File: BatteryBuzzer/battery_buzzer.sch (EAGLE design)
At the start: 20 parts, among them Q1 IRFML8244, Q2 IRFML8244, Q3 P-CHANNEL-MOSFETSOT23-3, Q4 P-CHANNEL-MOSFETSOT23-3, Q5 P-CHANNEL-MOSFETSOT23-3

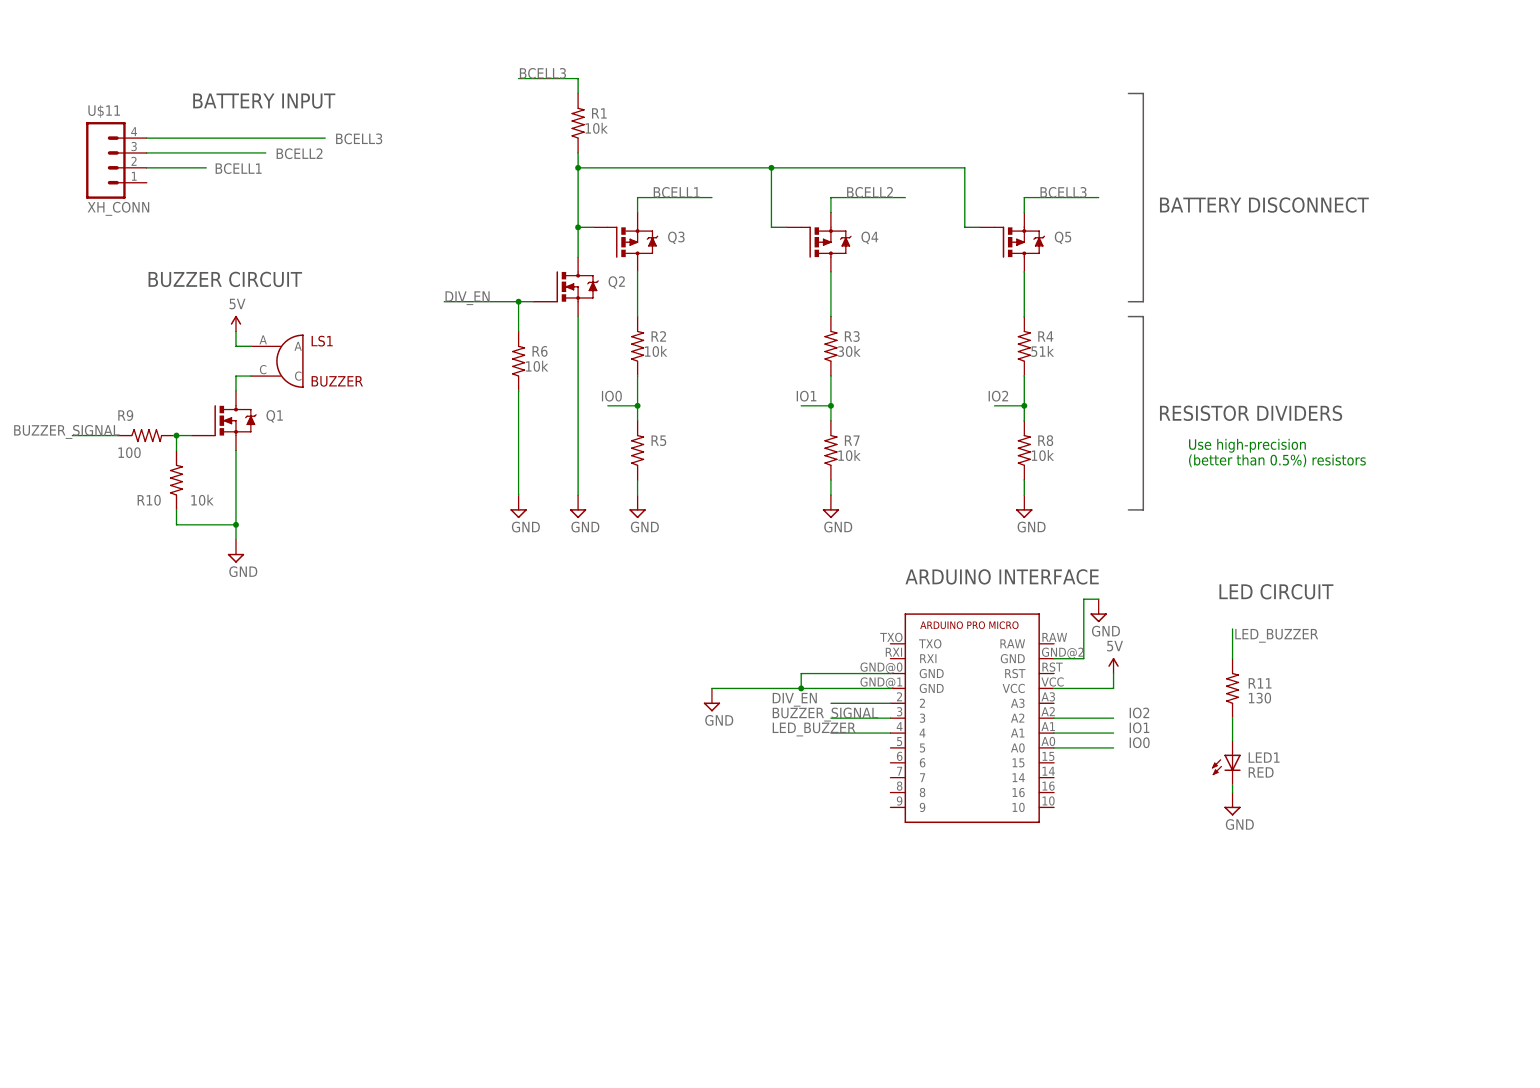
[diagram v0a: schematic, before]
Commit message: Added 7 segment array & calibration.
also nuked board file, it'd have to change too much anyway.

Have just enough I/O for the calibration button + calibration button
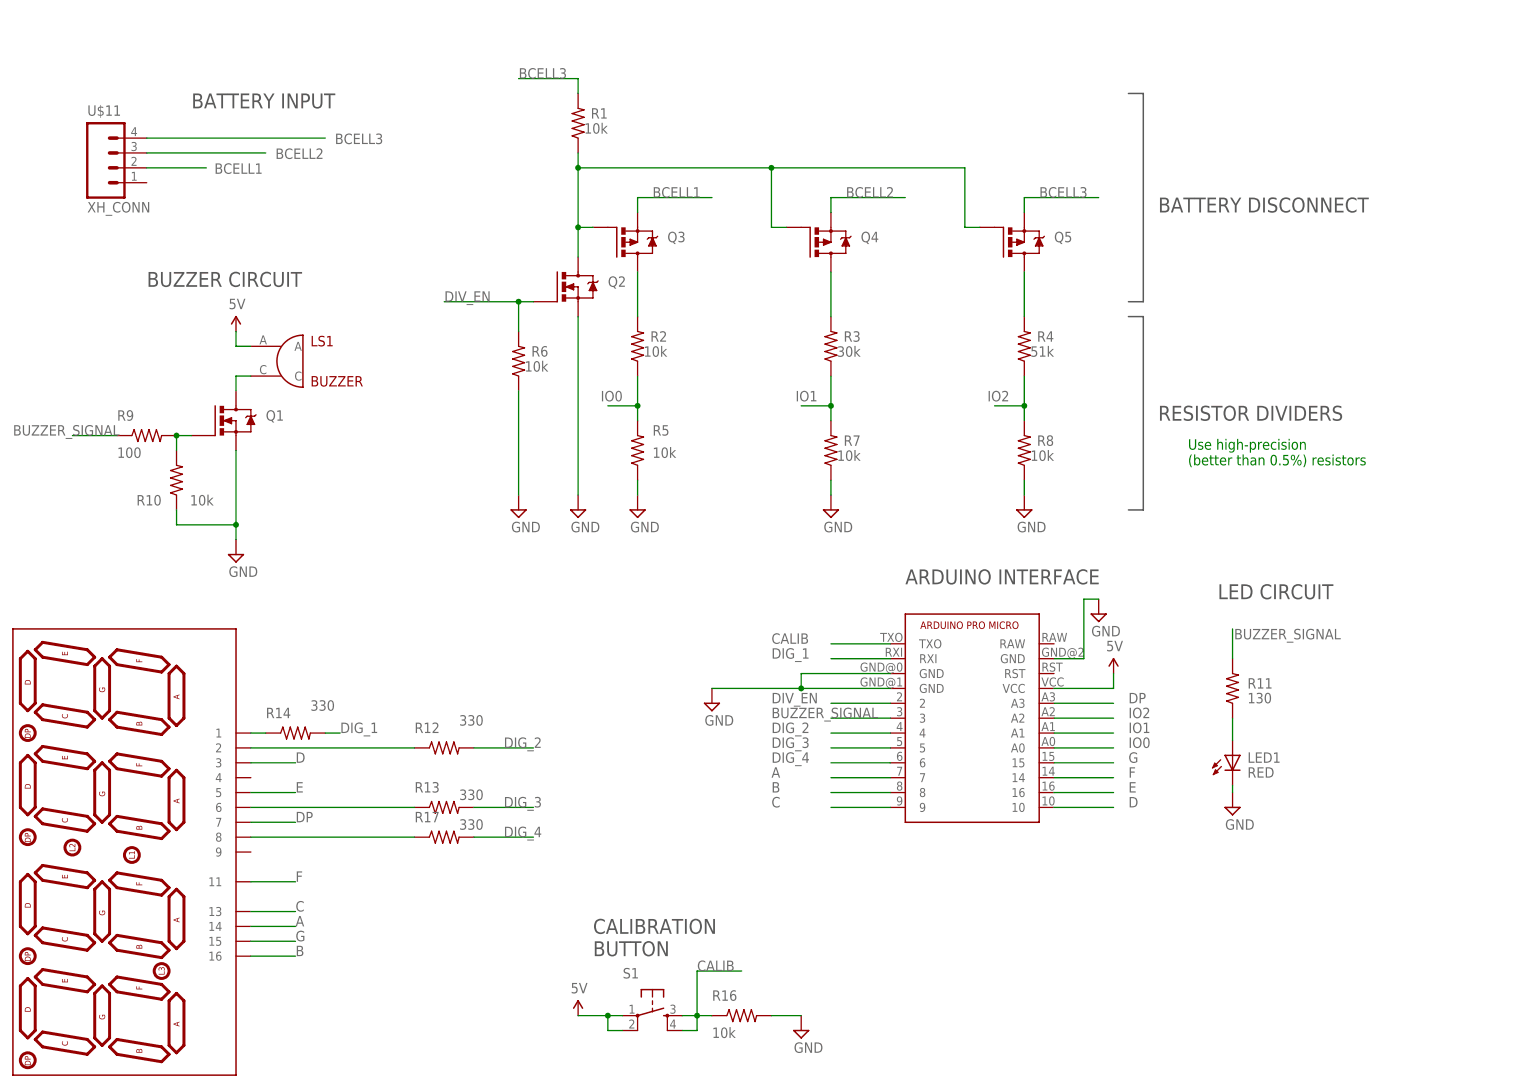
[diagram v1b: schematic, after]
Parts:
- added R12, R13, R14, R17: 330, pie:R-US_R0603
- added R16: 10k, pie:R-US_R0603
- added S1: (no value), pie:TAC_SWITCHPTH
- added U$6: 7-SEGMENT-4DIGIT, SparkFun-Displays:7-SEGMENT-4DIGIT
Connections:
- removed net LED_BUZZER: R11.2, U$5.4
- new net A: U$5.7, U$6.14
- new net B: U$5.8, U$6.16
- new net C: U$5.9, U$6.13
- new net CALIB: R16.1, S1.3, S1.4, U$5.TXO
- new net D: U$5.10, U$6.3
- new net DIG_1: R14.2, U$5.RXI
- new net DIG_2: R12.2, U$5.4
- new net DIG_3: R13.2, U$5.5
- new net DIG_4: R17.2, U$5.6
- new net DP: U$5.A3, U$6.7
- new net E: U$5.16, U$6.5
- new net F: U$5.14, U$6.11
- new net G: U$5.15, U$6.15
- new net N$10: R13.1, U$6.6
- new net N$12: R17.1, U$6.8
- new net N$14: R14.1, U$6.1
- new net N$8: R12.1, U$6.2
- net 5V: now also S1.1, S1.2
- net BUZZER_SIGNAL: now also R11.2
- net GND: now also R16.2
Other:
- note added: "CALIBRATION BUTTON"

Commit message: added DPST switch to libary, added power bypass to buzzer
power bypass so that with the push of a button the buzzer can turn out
powered by the battery alone.
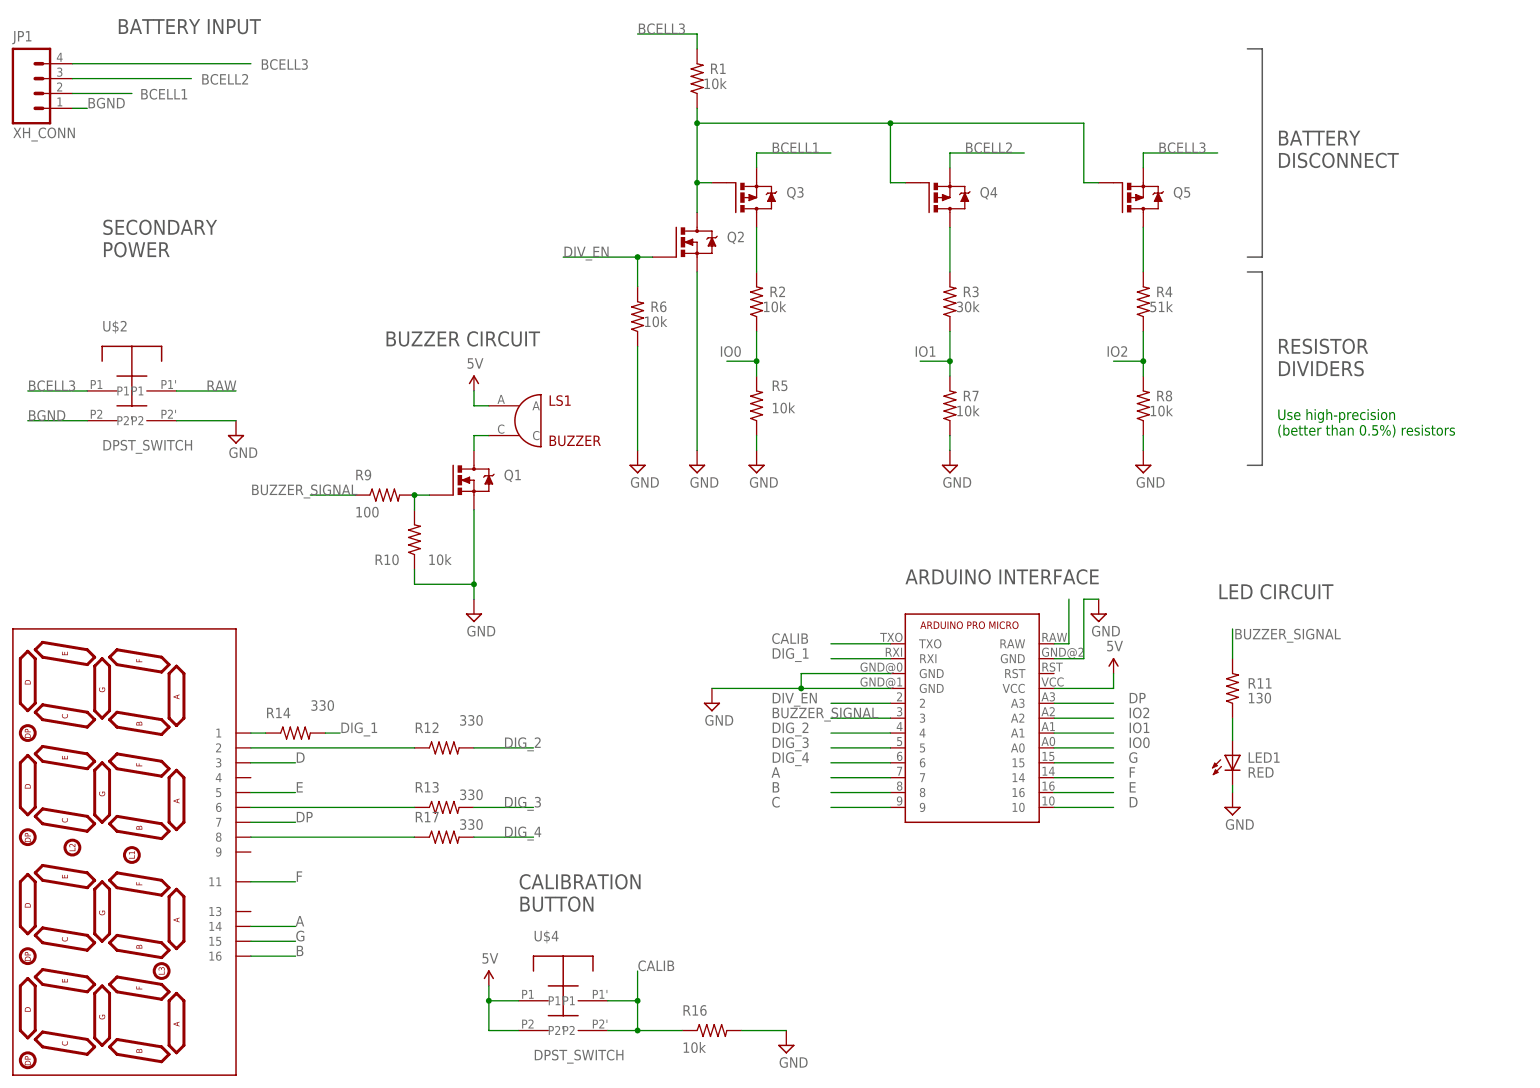
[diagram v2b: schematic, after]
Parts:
- removed S1: (no value), pie:TAC_SWITCHPTH
- removed U$11: XH_CONN, pie:XH_CONNECTOR_4POS
- added JP1: XH_CONN, pie:XH_CONNECTOR_4POS
- added U$2, U$4: DPST_SWITCH, pie:DPST_SWITCH
- renumbered U$5 to UC1, U$6 to DISP
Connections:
- new net BGND: JP1.1, U$2.P2
- new net RAW: U$2.P1', UC1.RAW
- net 5V: now also U$4.P1, U$4.P2; no longer S1.1, S1.2
- net BCELL1: now also JP1.2; no longer U$11.2
- net BCELL2: now also JP1.3; no longer U$11.3
- net BCELL3: now also JP1.4, U$2.P1; no longer U$11.4
- net C: no longer DISP.13
- net CALIB: now also U$4.P1', U$4.P2'; no longer S1.3, S1.4
- net GND: now also U$2.P2'
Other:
- note added: "DPST switch. Connect BCELL3 to RAW, which will get regulated on the arduino. Connect BGND to GND."
- note added: "SECONDARY POWER"
- moved on the sheet: LS1, Q1, Q2, Q3, Q4, Q5, R1, R10, R16, R2, R3, R4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

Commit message: final additions to the battery buzzer schematic
cleaned things up, added the obligatory debug features.
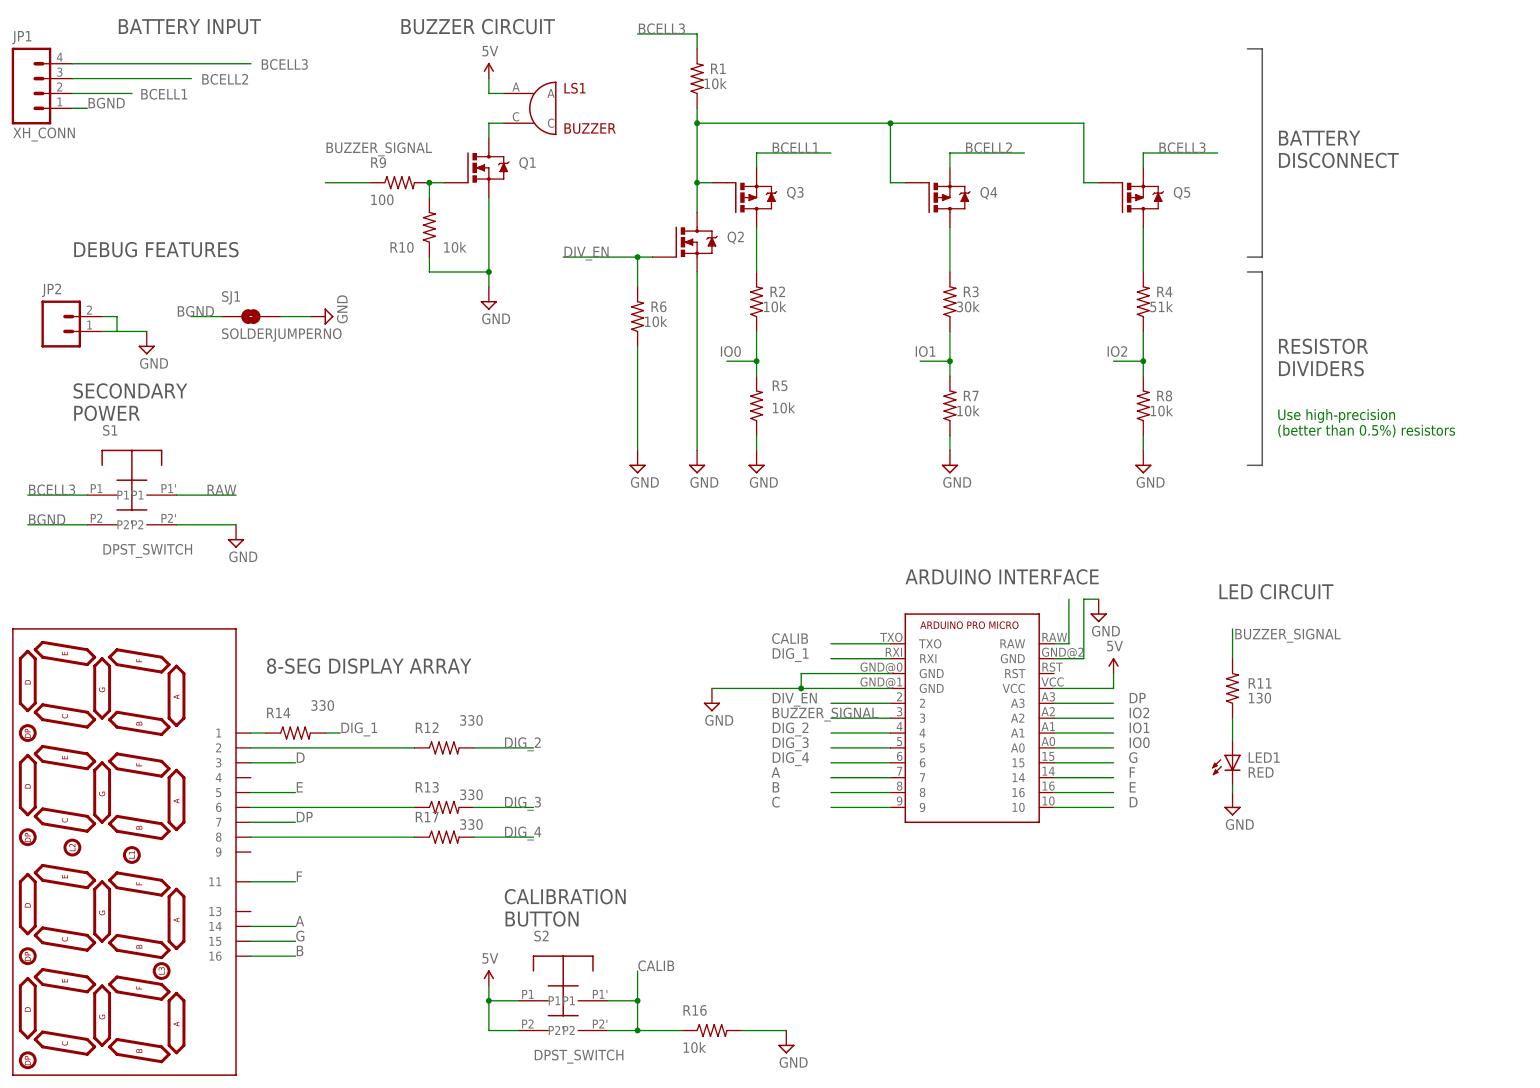
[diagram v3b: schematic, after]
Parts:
- removed U$2: DPST_SWITCH, pie:DPST_SWITCH
- added JP2: (no value), pie:M02PTH
- added S1: DPST_SWITCH, pie:DPST_SWITCH
- added SJ1: SOLDERJUMPERNO, pie:SOLDERJUMPERNO
- renumbered U$4 to S2
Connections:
- net BCELL3: now also S1.P1; no longer U$2.P1
- net BGND: now also S1.P2, SJ1.1; no longer U$2.P2
- net GND: now also JP2.1, JP2.2, S1.P2', SJ1.2; no longer U$2.P2'
- net RAW: now also S1.P1'; no longer U$2.P1'
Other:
- note added: "8-SEG DISPLAY ARRAY"
- note added: "Connect BCELL3 to RAW, which will get regulated on the arduino."
- note added: "DEBUG FEATURES"
- note removed: "DPST switch. Connect BCELL3 to RAW, which will get regulated on the arduino. Connect BGND to GND."
- note removed: "Do not connect ground pin on this battery leads unless it has a corrisponding reverse-plugin disconnect: it will short 12V to GND else"
- moved on the sheet: LS1, Q1, R10, R9

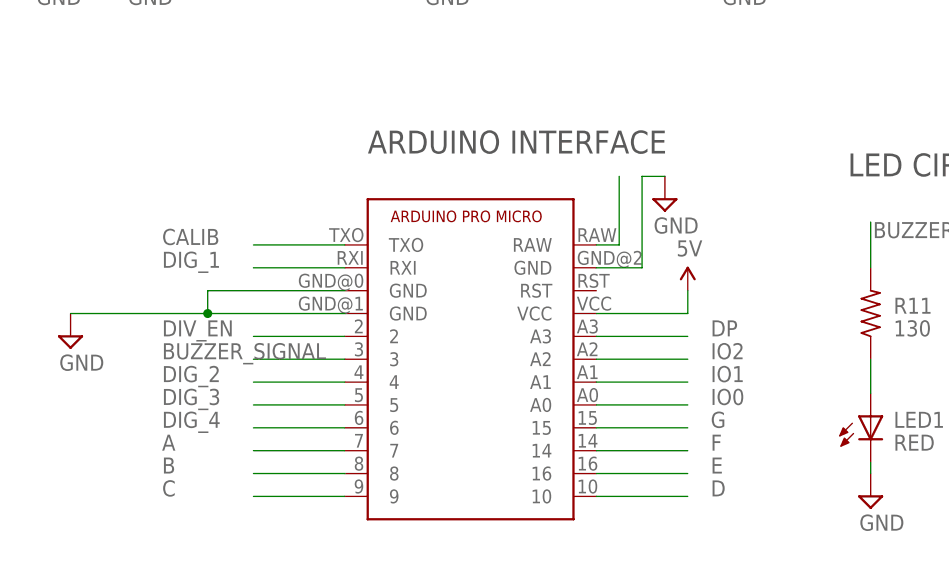
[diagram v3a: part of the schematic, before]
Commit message: some more pinremapping
to make routing easier... but routing starting now.
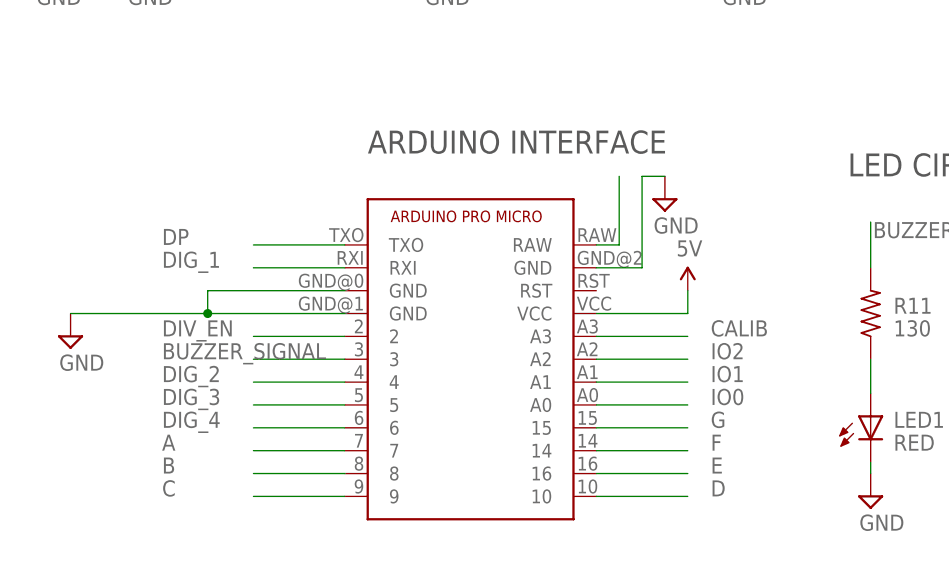
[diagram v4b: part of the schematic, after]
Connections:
- net CALIB: now also UC1.A3; no longer UC1.TXO
- net DP: now also UC1.TXO; no longer UC1.A3
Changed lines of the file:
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@@
 </segment>
 <segment>
-<pinref part="UC1" gate="G$1" pin="A3"/>
-<wire x1="180.34" y1="66.04" x2="190.5" y2="66.04" width="0.1524" layer="91"/>
-<label x="193.04" y="66.04" size="1.778" layer="95"/>
+<pinref part="UC1" gate="G$1" pin="TXO"/>
+<wire x1="152.4" y1="76.2" x2="142.24" y2="76.2" width="0.1524" layer="91"/>
+<label x="132.08" y="76.2" size="1.778" layer="95"/>
 </segment>
 </net>
@@
 </segment>
 <segment>
-<pinref part="UC1" gate="G$1" pin="TXO"/>
-<wire x1="152.4" y1="76.2" x2="142.24" y2="76.2" width="0.1524" layer="91"/>
-<label x="132.08" y="76.2" size="1.778" layer="95"/>
+<pinref part="UC1" gate="G$1" pin="A3"/>
+<wire x1="180.34" y1="66.04" x2="190.5" y2="66.04" width="0.1524" layer="91"/>
+<label x="193.04" y="66.04" size="1.778" layer="95"/>
 </segment>
 </net>

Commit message: initial layout.
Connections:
- net BUZZER_SIGNAL: now also UC1.RXI; no longer UC1.3
- net DIG_1: now also UC1.3; no longer UC1.RXI
- net DIV_EN: now also UC1.TXO; no longer UC1.2
- net DP: now also UC1.2; no longer UC1.TXO
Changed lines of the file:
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@@
-</segment>
-<segment>
-<pinref part="UC1" gate="G$1" pin="3"/>
-<wire x1="152.4" y1="63.5" x2="142.24" y2="63.5" width="0.1524" layer="91"/>
-<label x="132.08" y="63.5" size="1.778" layer="95"/>
 </segment>
 <segment>
@@
 <label x="211.074" y="76.962" size="1.778" layer="95"/>
 <pinref part="R11" gate="G$1" pin="2"/>
+</segment>
+<segment>
+<pinref part="UC1" gate="G$1" pin="RXI"/>
+<wire x1="152.4" y1="73.66" x2="142.24" y2="73.66" width="0.1524" layer="91"/>
+<label x="132.08" y="73.66" size="1.778" layer="95"/>
 </segment>
 </net>
@@
 </segment>
 <segment>
-<pinref part="UC1" gate="G$1" pin="2"/>
-<wire x1="152.4" y1="66.04" x2="142.24" y2="66.04" width="0.1524" layer="91"/>
-<label x="132.08" y="66.04" size="1.778" layer="95"/>
+<pinref part="UC1" gate="G$1" pin="TXO"/>
+<wire x1="152.4" y1="76.2" x2="142.24" y2="76.2" width="0.1524" layer="91"/>
+<label x="132.08" y="76.2" size="1.778" layer="95"/>
 </segment>
 </net>
@@
 </segment>
 <segment>
-<pinref part="UC1" gate="G$1" pin="RXI"/>
-<wire x1="152.4" y1="73.66" x2="142.24" y2="73.66" width="0.1524" layer="91"/>
-<label x="132.08" y="73.66" size="1.778" layer="95"/>
+<pinref part="UC1" gate="G$1" pin="3"/>
+<wire x1="152.4" y1="63.5" x2="142.24" y2="63.5" width="0.1524" layer="91"/>
+<label x="132.08" y="63.5" size="1.778" layer="95"/>
 </segment>
 </net>
@@
 </segment>
 <segment>
-<pinref part="UC1" gate="G$1" pin="TXO"/>
-<wire x1="152.4" y1="76.2" x2="142.24" y2="76.2" width="0.1524" layer="91"/>
-<label x="132.08" y="76.2" size="1.778" layer="95"/>
+<pinref part="UC1" gate="G$1" pin="2"/>
+<wire x1="152.4" y1="66.04" x2="142.24" y2="66.04" width="0.1524" layer="91"/>
+<label x="132.08" y="66.04" size="1.778" layer="95"/>
 </segment>
 </net>
